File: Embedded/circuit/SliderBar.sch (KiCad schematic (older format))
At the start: 1 part

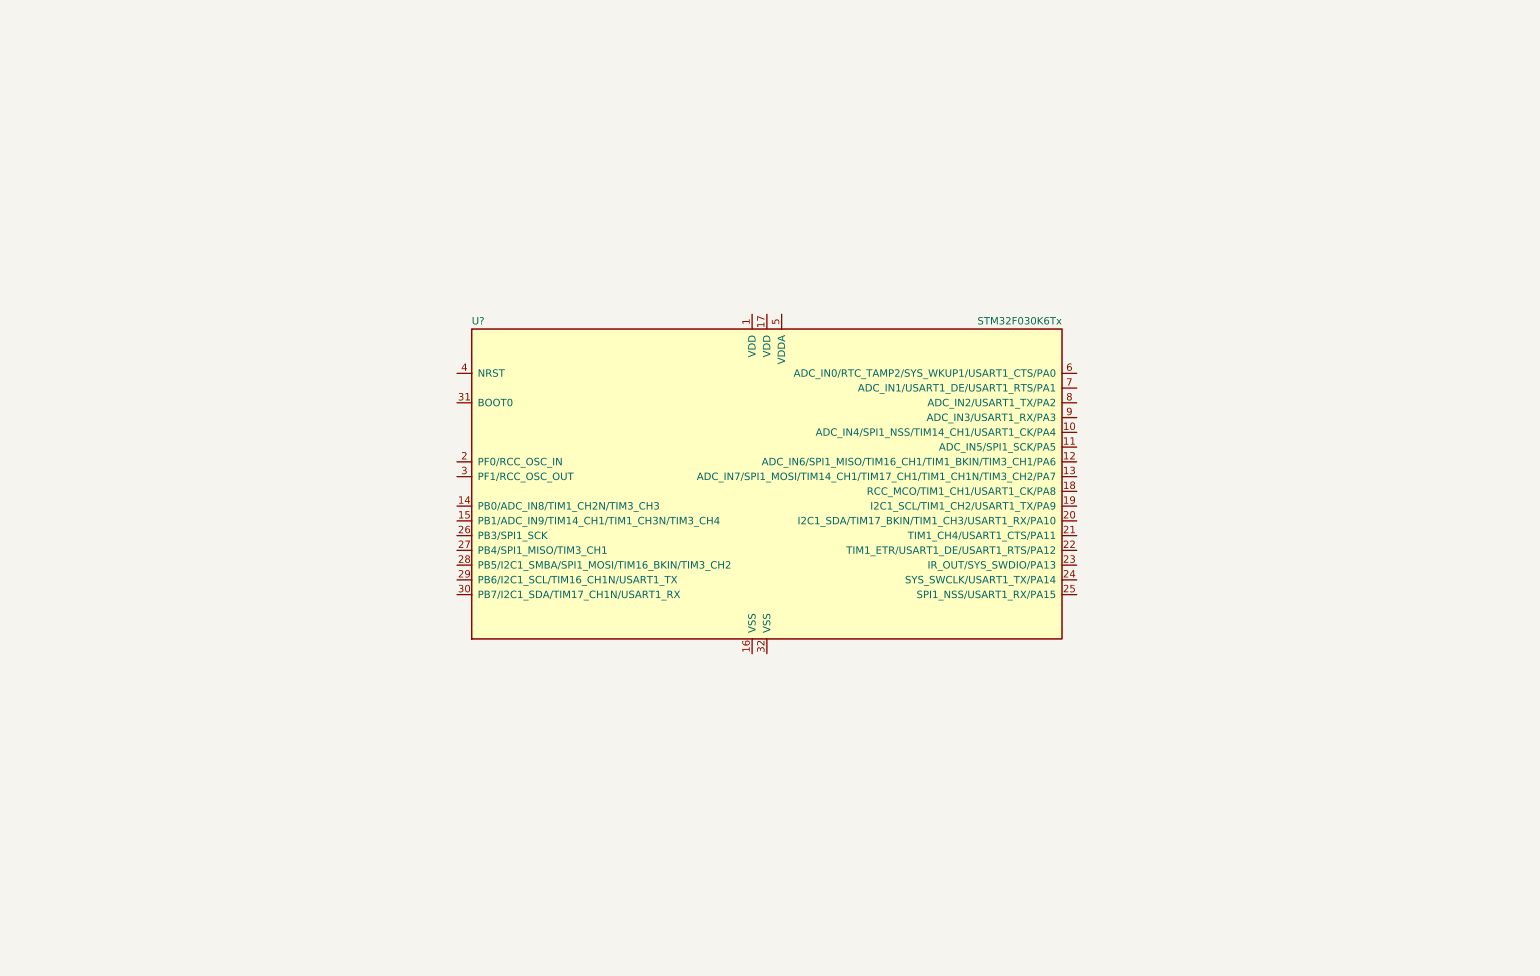
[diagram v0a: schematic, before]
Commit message: Update PCB, Add resist_at basic support
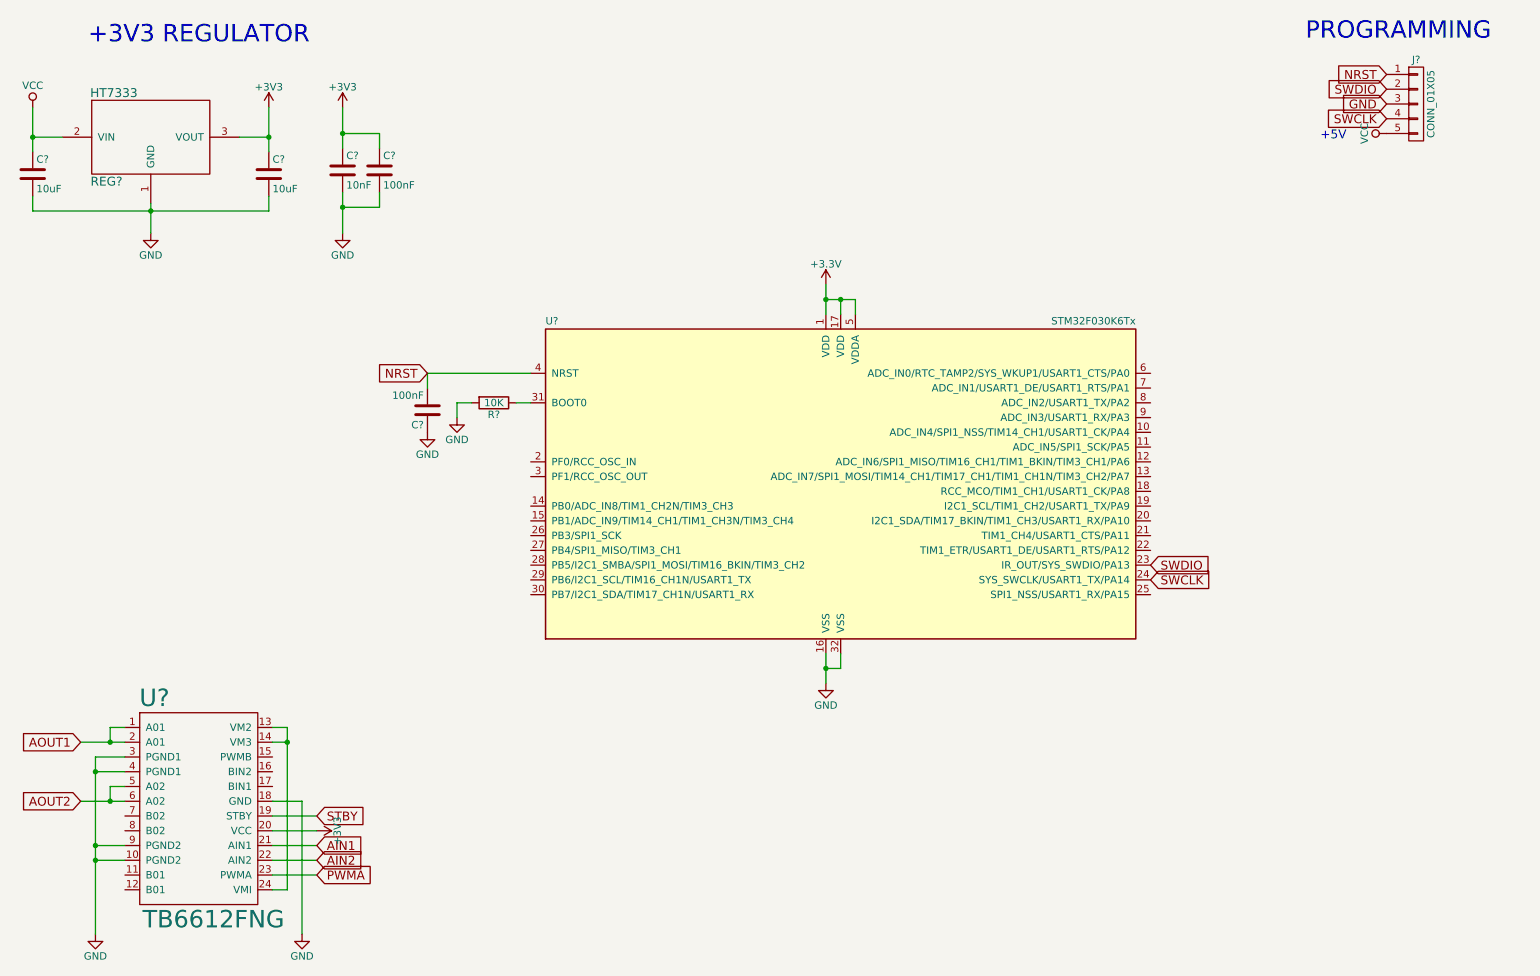
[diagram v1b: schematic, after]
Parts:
- added C? (x2): 100nF, symbol C
- added C? (x2): 10uF, symbol C
- added C?: 10nF, symbol C
- added J?: CONN_01X05, symbol CONN_01X05
- added R?: 10K, symbol R
- added REG?: HT7333, symbol HT7333
- added U?: TB6612FNG, Housings_SSOP:SSOP-24_5.3x8.2mm_Pitch0.65mm, symbol TB6612FNG
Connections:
- net +3V3: now reaches U?.1 (VDD)
- net +3V3: now also U?.17 (VDD), U?.5 (VDDA), C?.1, C?.1, C?.1, REG?.3 (VOUT), U?.20 (VCC)
- net GND: now reaches U?.16 (VSS)
- net GND: now also U?.32 (VSS), C?.1, C?.2, C?.2, C?.2, C?.2, J?.3 (P3), R?.2, REG?.1 (GND), U?.10 (PGND2), U?.18 (GND), U?.3 (PGND1), U?.4 (PGND1), U?.9 (PGND2)
- net SWDIO: now reaches U?.23 (IR_OUT/SYS_SWDIO/PA13)
- net SWDIO: now also J?.2 (P2)
- net SWCLK: now reaches U?.24 (SYS_SWCLK/USART1_TX/PA14)
- net SWCLK: now also J?.4 (P4)
- net at U?.31 (BOOT0): now also R?.1
- net NRST: now reaches U?.4 (NRST)
- net NRST: now also C?.2, J?.1 (P1)
- new net: U?.13 (VM2), U?.14 (VM3), U?.24 (VMI)
- new net AIN1: U?.21 (AIN1)
- new net AIN2: U?.22 (AIN2)
- new net AOUT1: U?.1 (A01), U?.2 (A01)
- new net AOUT2: U?.5 (A02), U?.6 (A02)
- new net PWMA: U?.23 (PWMA)
- new net STBY: U?.19 (STBY)
- new net VCC: C?.1, J?.5 (P5), REG?.2 (VIN)
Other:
- note added: "+3V3 REGULATOR"
- note added: "+5V"
- note added: "PROGRAMMING"
- moved on the sheet: U?

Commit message: Improve PID Performances & Add tracking filter & graphs
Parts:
- removed R?: 10K, symbol R
- added J?: CONN_01X02, symbol CONN_01X02
- added J?: CONN_01X03, symbol CONN_01X03
- added U?: FT232RL, SSOP-28, symbol FT232RL
- added USB?: USB_PLUG, symbol USB_PLUG
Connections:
- net +3V3: now also J?.1 (P1)
- net AOUT1: now also J?.1 (P1)
- net AOUT2: now also J?.2 (P2)
- net GND: now also J?.2 (P2), J?.3 (P3), U?.18 (GND), U?.21 (GND), U?.25 (AGND), U?.26 (TEST), U?.7 (GND); no longer J?.3 (P3)
- net NRST: now also J?.5 (P5); no longer J?.1 (P1)
- net SWCLK: now also J?.3 (P3); no longer J?.4 (P4)
- net SWDIO: now also J?.1 (P1); no longer J?.2 (P2)
- net VCC: now also J?.4 (P4); no longer J?.5 (P5)
- net DIV: now reaches U?.7 (ADC_IN1/USART1_DE/USART1_RTS/PA1)
- net DIV: now also J?.2 (P2)
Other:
- note added: "MOTOR HEADER"
- note added: "POTENTIOMETER"
- note removed: "+5V"
- moved on the sheet: J?
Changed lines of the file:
@@
 EELAYER 25 0
 EELAYER END
-$Descr A4 11693 8268
+$Descr A3 16535 11693
 encoding utf-8
 Sheet 1 1
@@
 	1    0    0    -1
 $EndComp
-$Comp
-L R R?
-U 1 1 5931E45A
-P 4150 3250
-F 0 "R?" V 4230 3250 50  0000 C CNN
-F 1 "10K" V 4150 3250 50  0000 C CNN
-F 2 "" V 4080 3250 50  0001 C CNN
-F 3 "" H 4150 3250 50  0001 C CNN
-	1    4150 3250
-	0    1    1    0
-$EndComp
-$Comp
-L GND #PWR03
-U 1 1 5931E54F
-P 3900 3350
-F 0 "#PWR03" H 3900 3100 50  0001 C CNN
-F 1 "GND" H 3900 3200 50  0000 C CNN
-F 2 "" H 3900 3350 50  0001 C CNN
-F 3 "" H 3900 3350 50  0001 C CNN
-	1    3900 3350
-	1    0    0    -1
-$EndComp
-Text GLabel 10200 1025 0    60   Input ~ 0
+Text GLabel 15150 1575 0    60   Input ~ 0
 NRST
 $Comp
 L CONN_01X05 J?
 U 1 1 5931E815
-P 10400 1225
-F 0 "J?" H 10400 1525 50  0000 C CNN
-F 1 "CONN_01X05" V 10500 1225 50  0000 C CNN
-F 2 "" H 10400 1225 50  0001 C CNN
-F 3 "" H 10400 1225 50  0001 C CNN
-	1    10400 1225
-	1    0    0    -1
-$EndComp
-Text GLabel 10200 1125 0    60   Input ~ 0
+P 15350 1375
+F 0 "J?" H 15350 1675 50  0000 C CNN
+F 1 "CONN_01X05" V 15450 1375 50  0000 C CNN
+F 2 "" H 15350 1375 50  0001 C CNN
+F 3 "" H 15350 1375 50  0001 C CNN
+	1    15350 1375
+	1    0    0    -1
+$EndComp
+Text GLabel 15150 1175 0    60   Input ~ 0
 SWDIO
-Text GLabel 10200 1225 0    60   Input ~ 0
-GND
-Text GLabel 10200 1325 0    60   Input ~ 0
+Text GLabel 15150 1375 0    60   Input ~ 0
 SWCLK
 Text GLabel 3700 3050 0    60   Input ~ 0
@@
 Text GLabel 8600 4450 2    60   Input ~ 0
 SWCLK
-$Comp
-L VCC #PWR05
-U 1 1 5932A93D
-P 10200 1425
-F 0 "#PWR05" H 10200 1275 50  0001 C CNN
-F 1 "VCC" H 10200 1575 50  0000 C CNN
-F 2 "" H 10200 1425 50  0001 C CNN
-F 3 "" H 10200 1425 50  0001 C CNN
-	1    10200 1425
-	0    -1   -1   0
-$EndComp
-Text Notes 9750 1475 0    60   ~ 0
-+5V
-Text Notes 9650 800  0    118  ~ 0
+Text Notes 14375 950  0    118  ~ 0
 PROGRAMMING
 Text Notes 1400 825  0    118  ~ 0
@@
 	6500 2650 6500 2550
 Connection ~ 6500 2550
-Wire Wire Line
-	4400 3250 4300 3250
-Wire Wire Line
-	4000 3250 3900 3250
-Wire Wire Line
-	3900 3250 3900 3350
 Wire Wire Line
 	4400 3050 3700 3050
@@
 Text GLabel 2950 6050 2    60   Input ~ 0
 STBY
+$Comp
+L CONN_01X02 J?
+U 1 1 5933F201
+P 15250 2450
+F 0 "J?" H 15250 2600 50  0000 C CNN
+F 1 "CONN_01X02" V 15350 2450 50  0000 C CNN
+F 2 "" H 15250 2450 50  0001 C CNN
+F 3 "" H 15250 2450 50  0001 C CNN
+	1    15250 2450
+	1    0    0    -1
+$EndComp
+Text Notes 14325 2075 0    118  ~ 0
+MOTOR HEADER
+Text GLabel 15050 2400 0    60   Input ~ 0
+AOUT1
+Text GLabel 15050 2500 0    60   Input ~ 0
+AOUT2
+Text Notes 14300 3000 0    118  ~ 0
+POTENTIOMETER
+$Comp
+L CONN_01X03 J?
+U 1 1 5933FA55
+P 15275 3475
+F 0 "J?" H 15275 3675 50  0000 C CNN
+F 1 "CONN_01X03" V 15375 3475 50  0000 C CNN
+F 2 "" H 15275 3475 50  0001 C CNN
+F 3 "" H 15275 3475 50  0001 C CNN
+	1    15275 3475
+	1    0    0    -1
+$EndComp
+$Comp
+L GND #PWR?
+U 1 1 5933FBA0
+P 15075 3575
+F 0 "#PWR?" H 15075 3325 50  0001 C CNN
+F 1 "GND" H 15075 3425 50  0000 C CNN
+F 2 "" H 15075 3575 50  0001 C CNN
+F 3 "" H 15075 3575 50  0001 C CNN
+	1    15075 3575
+	1    0    0    -1
+$EndComp
+$Comp
+L +3V3 #PWR?
+U 1 1 5933FBCC
+P 15075 3375
+F 0 "#PWR?" H 15075 3225 50  0001 C CNN
+F 1 "+3V3" H 15075 3515 50  0000 C CNN
+F 2 "" H 15075 3375 50  0001 C CNN
+F 3 "" H 15075 3375 50  0001 C CNN
+	1    15075 3375
+	1    0    0    -1
+$EndComp
+Text GLabel 15075 3475 0    60   Input ~ 0
+DIV
+Text GLabel 8600 3150 2    60   Input ~ 0
+DIV
+$Comp
+L GND #PWR?
+U 1 1 596B846D
+P 14700 1175
+F 0 "#PWR?" H 14700 925 50  0001 C CNN
+F 1 "GND" H 14700 1025 50  0000 C CNN
+F 2 "" H 14700 1175 50  0001 C CNN
+F 3 "" H 14700 1175 50  0001 C CNN
+	1    14700 1175
+	-1   0    0    1
+$EndComp
+$Comp
+L VCC #PWR?
+U 1 1 596B8497
+P 14600 1175
+F 0 "#PWR?" H 14600 1025 50  0001 C CNN
+F 1 "VCC" H 14600 1325 50  0000 C CNN
+F 2 "" H 14600 1175 50  0001 C CNN
+F 3 "" H 14600 1175 50  0001 C CNN
+	1    14600 1175
+	1    0    0    -1
+$EndComp
+Wire Wire Line
+	14700 1175 14700 1275
+Wire Wire Line
+	14700 1275 15150 1275
+Wire Wire Line
+	14600 1175 14600 1475
+Wire Wire Line
+	14600 1475 15150 1475
+$Comp
+L FT232RL U?
+U 1 1 596B951E
+P 9225 7950
+F 0 "U?" H 8575 8850 50  0000 L CNN
+F 1 "FT232RL" H 9625 8850 50  0000 L CNN
+F 2 "SSOP-28" H 9225 7950 50  0001 C CNN
+F 3 "" H 9225 7950 50  0001 C CNN
+	1    9225 7950
+	1    0    0    -1
+$EndComp
+$Comp
+L GND #PWR?
+U 1 1 596B963D
+P 8325 8750
+F 0 "#PWR?" H 8325 8500 50  0001 C CNN
+F 1 "GND" H 8325 8600 50  0000 C CNN
+F 2 "" H 8325 8750 50  0001 C CNN
+F 3 "" H 8325 8750 50  0001 C CNN
+	1    8325 8750
+	1    0    0    -1
+$EndComp
+$Comp
+L GND #PWR?
+U 1 1 596B9675
+P 9025 9150
+F 0 "#PWR?" H 9025 8900 50  0001 C CNN
+F 1 "GND" H 9025 9000 50  0000 C CNN
+F 2 "" H 9025 9150 50  0001 C CNN
+F 3 "" H 9025 9150 50  0001 C CNN
+	1    9025 9150
+	1    0    0    -1
+$EndComp
+Wire Wire Line
+	9025 8950 9025 9150
+Wire Wire Line
+	9225 8950 9225 9050
+Wire Wire Line
+	9025 9050 9425 9050
+Connection ~ 9025 9050
+Wire Wire Line
+	9425 9050 9425 8950
+Connection ~ 9225 9050
+Wire Wire Line
+	9325 8950 9325 9050
+Connection ~ 9325 9050
+Wire Wire Line
+	8425 8650 8325 8650
+Wire Wire Line
+	8325 8650 8325 8750
+$Comp
+L USB_PLUG USB?
+U 1 1 596BA032
+P 13625 7100
+F 0 "USB?" H 13445 7225 60  0000 C CNN
+F 1 "USB_PLUG" H 13560 7320 60  0000 C CNN
+F 2 "" H 13625 7100 60  0001 C CNN
+F 3 "" H 13625 7100 60  0001 C CNN
+	1    13625 7100
+	0    1    1    0
+$EndComp
+$Comp
+L GND #PWR?
+U 1 1 596BA42F
+P 13150 6775
+F 0 "#PWR?" H 13150 6525 50  0001 C CNN
+F 1 "GND" H 13150 6625 50  0000 C CNN
+F 2 "" H 13150 6775 50  0001 C CNN
+F 3 "" H 13150 6775 50  0001 C CNN
+	1    13150 6775
+	-1   0    0    1
+$EndComp
 $EndSCHEMATC
